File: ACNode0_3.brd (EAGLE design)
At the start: 100 x 65 mm, 85 parts, among them IC1 74AHC1G04DCK, IC2 MC78M05CDTG, IC3 LM1117IMP-3.3, J1 POWER_JACKPTH, K1 351, K2 351, T1 MMBT4401, T2 MMBT4401, U2 MAGJACK-POE, U3 CLAMP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

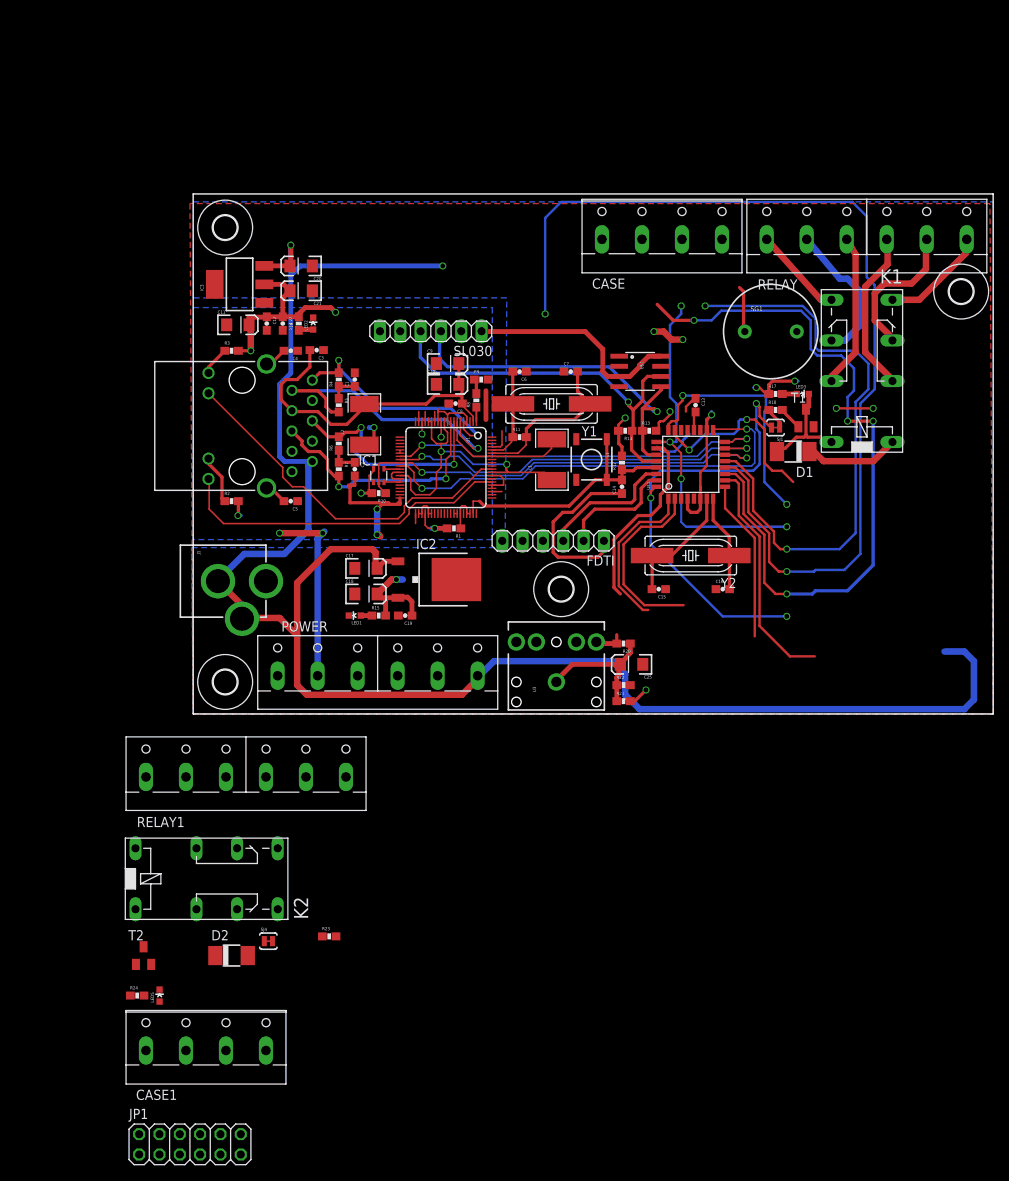
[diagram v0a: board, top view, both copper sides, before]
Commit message: layout sans poe
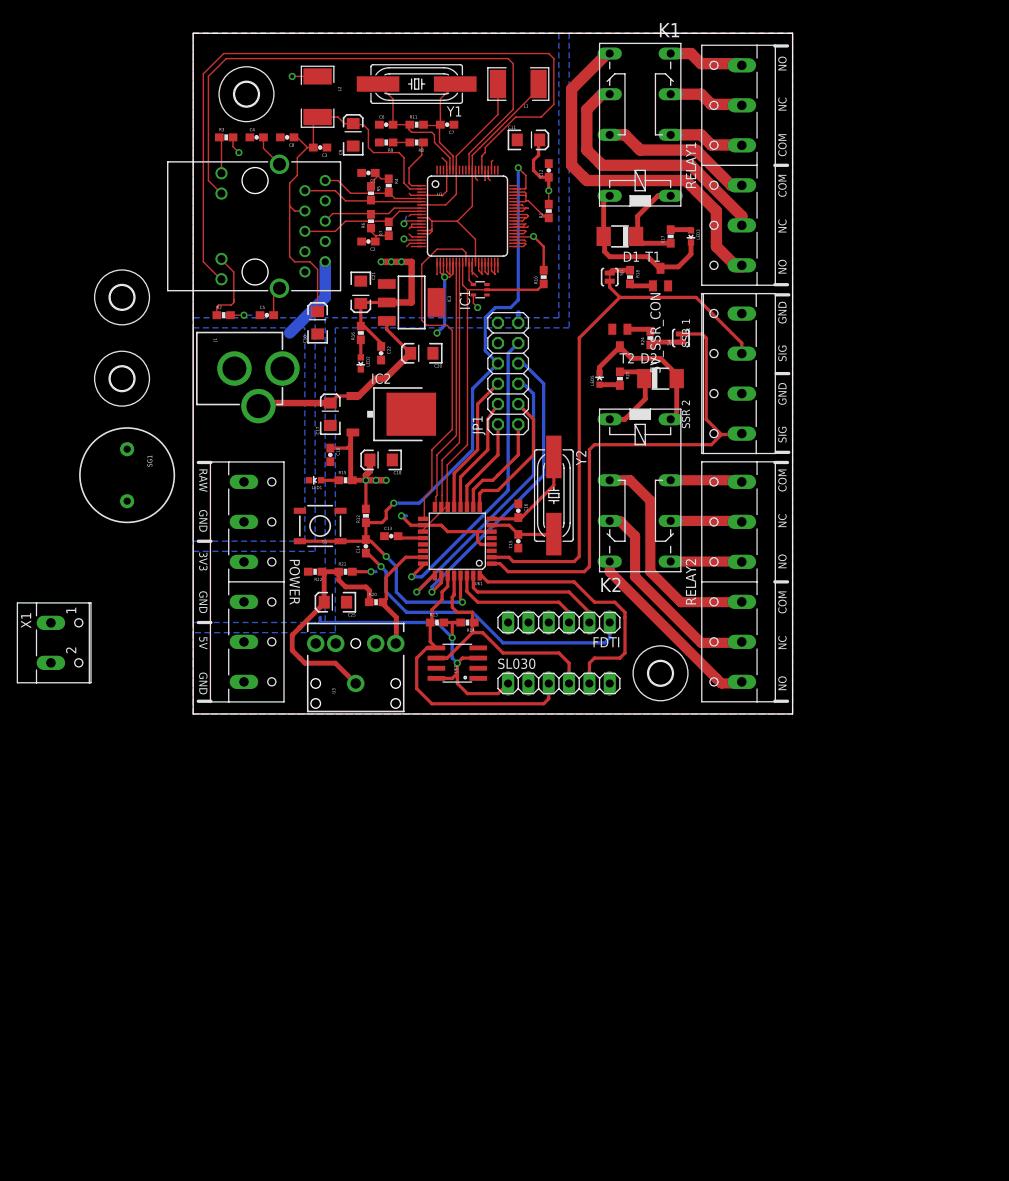
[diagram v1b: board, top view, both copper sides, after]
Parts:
- removed CASE, CASE1: (no value), con-wago-500:W237-4
- removed RELAY: (no value), con-wago-500:W237-6
- added 5V_SSR_CON: (no value), con-wago-500:W237-4
- added RELAY2: (no value), con-wago-500:W237-6
- added X1: (no value), con-wago-500:W237-102
- moved R24 104.3 mm to (57.1, 47.0), turned to 90 degrees
- moved JP1 104.2 mm to (39.4, 42.5), turned to 90 degrees
- moved T2 97.5 mm to (53.3, 47.0), turned to 180 degrees
- moved RELAY1 96.6 mm to (67.3, 68.6), turned to 90 degrees
- moved LED5 94.7 mm to (50.8, 41.9)
- moved H2 92.7 mm to (6.67, 77.5)
- moved SJ4 91.3 mm to (61.0, 47.0), turned to 90 degrees
- moved D2 89.9 mm to (58.4, 41.9)
- moved SG1 82.4 mm to (-8.26, 29.8), turned to 270 degrees
- moved K2 79.9 mm to (55.9, 33.0), turned to 270 degrees
- moved R23 78.6 mm to (53.3, 41.9), turned to 270 degrees
- moved H4 49.8 mm to (-8.89, 52.1)
- moved L1 47.1 mm to (40.6, 78.7), turned to 180 degrees
- moved SL030 46.9 mm to (45.7, 3.81), turned to 0 degrees
- moved Y1 43.4 mm to (27.9, 78.7)
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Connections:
- removed net N$44: K2.P2, RELAY1.3
- removed net N$45: K2.P1, RELAY1.4
- new net N$23: K2.P1, RELAY2.3
- new net N$36: K2.P2, RELAY2.6
- net +3V3: now also POWER.4, R13.2, R14.2; no longer POWER.2
- net A1: now also JP1.9; no longer JP1.3
- net A2: now also JP1.5; no longer JP1.2
- net A3: now also JP1.7; no longer JP1.1
- net A6: now also SG1.-; no longer CASE1.1, SJ1.2
- net A7: now also X1.1; no longer CASE1.3, SJ4.2
- net D2: now also SL030.5; no longer JP1.7
- net D3: now also 5V_SSR_CON.1, SJ4.2; no longer JP1.6
- net D4: now also 5V_SSR_CON.3, SJ1.2; no longer JP1.5
- net D5: now also JP1.3; no longer CASE.1
- net D6: now also JP1.1; no longer SL030.5
- net D7: now also JP1.2; no longer JP1.9
- net D8: now also JP1.4; no longer JP1.8
- net D9: now also JP1.6; no longer SG1.-
- net GND: now also 5V_SSR_CON.2, 5V_SSR_CON.4, X1.2; no longer CASE.2, CASE1.2, CASE1.4
- net N$25: now also RELAY1.1; no longer RELAY.1
- net N$27: now also RELAY1.2; no longer RELAY.2
- net N$29: now also RELAY1.3; no longer RELAY.3
- net N$30: now also RELAY1.4; no longer RELAY.4
- net N$31: now also RELAY1.5; no longer RELAY.5
- net N$32: now also RELAY1.6; no longer RELAY.6
- net N$42: now also RELAY2.4; no longer RELAY1.1
- net N$43: now also RELAY2.5; no longer RELAY1.2
- net N$46: now also RELAY2.2; no longer RELAY1.5
- net N$47: now also RELAY2.1; no longer RELAY1.6
- net RAW: now also POWER.2; no longer POWER.6
- net RESET: now also JP1.8; no longer JP1.4
- net VCC: now also POWER.6; no longer POWER.4, R13.2, R14.2
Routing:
- net RAW: track 224.1 -> 38.6 mm, vias 2 -> 0
- net D8: track 124.9 -> 14.6 mm, vias 2 -> 0
- net D7: track 91.3 -> 11.9 mm, vias 4 -> 0
- net RESET: track 32.6 -> 93.3 mm, vias 0 -> 4
- net D9: track 78.0 -> 17.7 mm, vias 2 -> 0
- net N$17: track 42.4 -> 91.3 mm
- net D4: track 23.5 -> 67.5 mm
- net D3: track 19.9 -> 63.8 mm
- net N$25: track 11.5 -> 45.5 mm
- net GND: track 52.9 -> 82.9 mm
- net N$23: track 0.00 -> 28.0 mm
- net N$46: track 0.00 -> 25.8 mm
- net N$16: track 45.7 -> 70.2 mm
- net D2: track 56.6 -> 32.7 mm, vias 3 -> 0
- net N$47: track 0.00 -> 23.6 mm
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- added copper zone on layer 16, net RAW
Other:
- board size 100 x 65 mm -> 74.9 x 85.1 mm
- board text added: "3V3"
- board text added: "5V"
- board text added: "COM"
- board text added: "GND"
- board text added: "NC"
- board text added: "NO"
- board text added: "RAW"
- board text added: "SIG"
- board text added: "SSR 1"
- board text added: "SSR 2"
